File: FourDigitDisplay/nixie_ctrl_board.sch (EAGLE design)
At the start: 0 parts

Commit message: 制御基板の初版
まだニキシー管を配置しただけ
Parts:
- added H1, H2, H3, H4: MOUNT_HOLE_3.2, Generic:MOUNT_HOLE_3.2
- added Q1, Q2, Q3, Q4: IN-12B, Parts:IN-12B
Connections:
- new net A_1: Q1.1
- new net A_2: Q2.1
- new net A_3: Q3.1
- new net A_4: Q4.1
- new net K1_0: Q1.2, Q2.2
- new net K1_1: Q1.11, Q2.11
- new net K1_2: Q1.10, Q2.10
- new net K1_3: Q1.9, Q2.9
- new net K1_4: Q1.8, Q2.8
- new net K1_5: Q1.7, Q2.7
- new net K1_6: Q1.6, Q2.6
- new net K1_7: Q1.5, Q2.5
- new net K1_8: Q1.4, Q2.4
- new net K1_9: Q1.3, Q2.3
- new net K1_D: Q1.12, Q2.12
- new net K2_0: Q3.2, Q4.2
- new net K2_1: Q3.11, Q4.11
- new net K2_2: Q3.10, Q4.10
- new net K2_3: Q3.9, Q4.9
- new net K2_4: Q3.8, Q4.8
- new net K2_5: Q3.7, Q4.7
- new net K2_6: Q3.6, Q4.6
- new net K2_7: Q3.5, Q4.5
- new net K2_8: Q3.4, Q4.4
- new net K2_9: Q3.3, Q4.3
- new net K2_D: Q3.12, Q4.12

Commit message: IC群を追加して仮置き
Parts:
- added CN1: PIC_CN_H, Connectors:PIC_CN_H
- added CN2: I2C_IF, PartsForProto:I2C_IF
- added R1, R2, R8, R9: 20k, Parts:RESISTOR_300MIL
- added R11, R12, R3, R4: 470, Parts:RESISTOR_300MIL
- added U1, U3: TLP627-2, Parts:TLP627-2
- added U2, U4: SN74141, Parts:SN74141
- added U5: PIC16F18857-I/SP, Parts:PIC16F18857-I/SP
- H1, H2, H3, H4, Q1, Q2, Q3, Q4: OC_NEWARK (none) -> unknown
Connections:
- new net +24V: R1.2, R2.2, R8.2, R9.2
- new net +5V: U2.VCC, U4.VCC
- new net 0V: U1G$1.C, U1G$2.C, U2.GND, U3G$1.C, U3G$2.C, U4.GND
- new net A1_CTL: R11.1
- new net A2_CTL: R12.1
- new net A3_CTL: R3.1
- new net A4_CTL: R4.1
- new net N$1: R1.1, U1G$1.COL
- new net N$11: R8.1, U3G$1.COL
- new net N$12: R9.1, U3G$2.COL
- new net N$13: R11.2, U3G$1.A
- new net N$14: R12.2, U3G$2.A
- new net N$2: R2.1, U1G$2.COL
- new net N$3: R3.2, U1G$1.A
- new net N$4: R4.2, U1G$2.A
- new net PIC_A1: U2.A
- new net PIC_A2: U4.A
- new net PIC_B1: U2.B
- new net PIC_B2: U4.B
- new net PIC_C1: U2.C
- new net PIC_C2: U4.C
- new net PIC_D1: U2.D
- new net PIC_D2: U4.D
- net A_1: now also U3G$1.EMIT
- net A_2: now also U3G$2.EMIT
- net A_3: now also U1G$1.EMIT
- net A_4: now also U1G$2.EMIT
- net K1_0: now also U2.0
- net K1_1: now also U2.1
- net K1_2: now also U2.2
- net K1_3: now also U2.3
- net K1_4: now also U2.4
- net K1_5: now also U2.5
- net K1_6: now also U2.6
- net K1_7: now also U2.7
- net K1_8: now also U2.8
- net K1_9: now also U2.9
- net K2_0: now also U4.0
- net K2_1: now also U4.1
- net K2_2: now also U4.2
- net K2_3: now also U4.3
- net K2_4: now also U4.4
- net K2_5: now also U4.5
- net K2_6: now also U4.6
- net K2_7: now also U4.7
- net K2_8: now also U4.8
- net K2_9: now also U4.9
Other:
- moved on the sheet: H1, H2, H3, H4

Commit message: 配線の追加
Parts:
- added C1: 0.1uF, Parts:CAP_100MIL
- added CN3, CN4: POWER_IF, PartsForProto:POWER_IF
- added R5: 10k, Parts:RESISTOR_300MIL
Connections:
- new net N$15: CN1.VSS, U5.VSS
- new net N$5: CN2.SDA, U5.RC4/SDA
- new net N$6: CN2.SCL, U5.RC3/SCL
- new net N$7: CN1.VPP/!MCLR, R5.1, U5.!MCLR!/RE3
- new net N$8: CN1.PGD, U5.RB7/PDAT
- new net N$9: CN1.PGC, U5.RB6/PCLK
- net +24V: now also CN3.VDD
- net +5V: now also C1.1, CN1.VDD, CN2.VDD, CN4.VDD, R5.2, U5.VDD
- net 0V: now also C1.2, CN2.GND, CN3.GND, CN4.GND, U5.VSS1
- net A1_CTL: now also U5.RA4
- net A2_CTL: now also U5.RA5
- net A3_CTL: now also U5.RB4
- net A4_CTL: now also U5.RB5
- net K1_D: now also U5.RC0
- net K2_D: now also U5.RC1
- net PIC_A1: now also U5.RA0
- net PIC_A2: now also U5.RB0
- net PIC_B1: now also U5.RA1
- net PIC_B2: now also U5.RB1
- net PIC_C1: now also U5.RA2
- net PIC_C2: now also U5.RB2
- net PIC_D1: now also U5.RA3
- net PIC_D2: now also U5.RB3
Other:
- moved on the sheet: CN1, CN2, H1, H2, H3, H4, Q1, Q2, Q3, Q4, R1, R11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

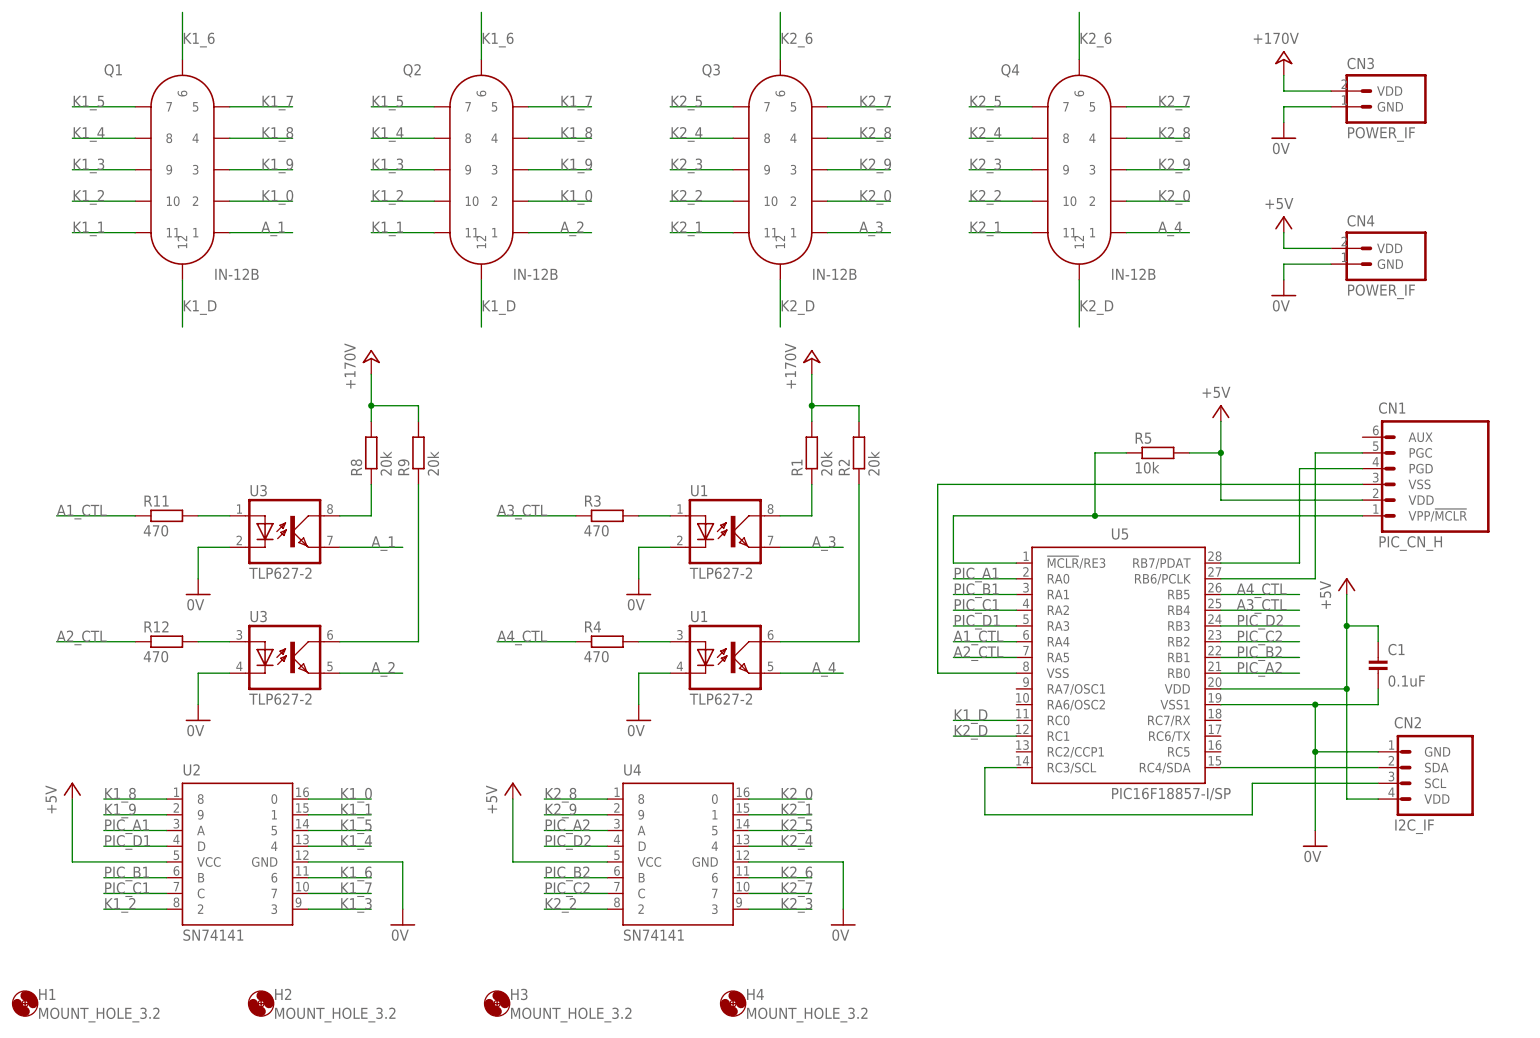
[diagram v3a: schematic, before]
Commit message: 部品配置修正
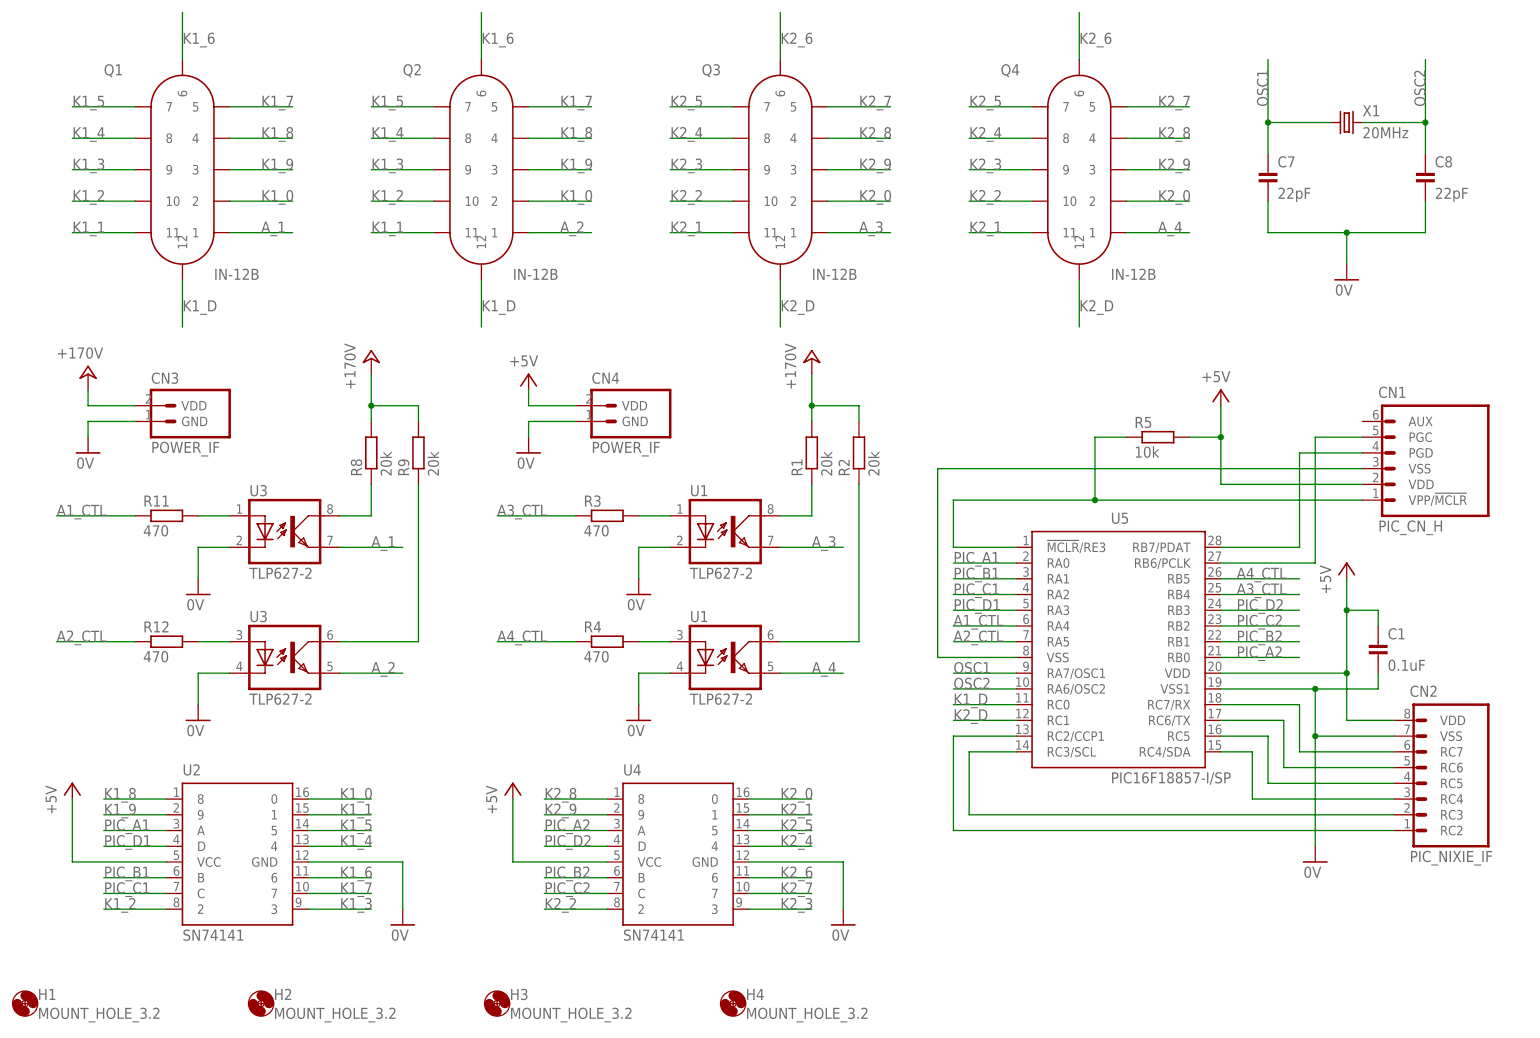
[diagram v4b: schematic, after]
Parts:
- added C7, C8: 22pF, Parts:CAP_100MIL
- added X1: 20MHz, Parts:HUSG-20.000-20
- CN2: value I2C_IF -> PIC_NIXIE_IF; device PartsForProto:I2C_IF -> PartsForProto:PIC_NIXIE_IF
- R11, R12, R3, R4, R5: device Parts:RESISTOR_300MIL -> Parts:RESISTOR_200MIL
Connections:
- new net N$10: CN2.RC5, U5.RC5
- new net N$16: CN2.RC4, U5.RC4/SDA
- new net N$17: CN2.RC3, U5.RC3/SCL
- new net N$18: CN2.RC2, U5.RC2/CCP1
- new net OSC1: C7.1, U5.RA7/OSC1, X1.1
- new net OSC2: C8.1, U5.RA6/OSC2, X1.2
- net 0V: now also C7.2, C8.2, CN2.VSS; no longer CN2.GND
- net N$5: now also CN2.RC7, U5.RC7/RX; no longer CN2.SDA, U5.RC4/SDA
- net N$6: now also CN2.RC6, U5.RC6/TX; no longer CN2.SCL, U5.RC3/SCL
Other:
- moved on the sheet: C1, CN1, CN3, CN4, R5, U5
